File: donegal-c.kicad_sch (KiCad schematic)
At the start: 178 parts, among them J2 ISP, SW1 SW_SPST, SW10 SW_SPST, SW11 SW_SPST, SW12 SW_SPST, SW13 SW_SPST, SW14 SW_SPST, SW15 SW_SPST, SW16 SW_SPST, SW17 SW_SPST, SW18 SW_SPST, SW19 SW_SPST, SW2 SW_SPST, SW20 SW_SPST, SW21 SW_SPST, SW22 SW_SPST, SW23 SW_SPST, SW24 SW_SPST, SW25 SW_SPST, SW26 SW_SPST, SW27 SW_SPST, SW28 SW_SPST, SW29 SW_SPST, SW3 SW_SPST, SW30 SW_SPST, SW31 SW_SPST, SW32 SW_SPST, SW33 SW_SPST, SW34 SW_SPST, SW35 SW_SPST, SW36 SW_SPST, SW37 SW_SPST, SW38 SW_SPST, SW39 SW_SPST, SW4 SW_SPST, SW40 SW_SPST, SW41 SW_SPST, SW42 SW_SPST, SW43 SW_SPST, SW44 SW_SPST, SW45 SW_SPST, SW46 SW_SPST, SW47 SW_SPST, SW48 SW_SPST, SW49 SW_SPST, SW5 SW_SPST, SW50 SW_SPST, SW51 SW_SPST, SW52 SW_SPST, SW53 SW_SPST, SW54 SW_SPST, SW55 SW_SPST, SW56 SW_SPST, SW57 SW_SPST, SW58 SW_SPST, SW59 SW_SPST, SW6 SW_SPST, SW60 SW_SPST, SW61 SW_SPST, SW62 SW_SPST, SW63 SW_SPST, SW64 SW_SPST, SW65 SW_SPST, SW66 SW_SPST, SW67 SW_SPST, SW68 RESET, SW69 BOOT, SW7 SW_SPST, SW70 SW_SPST, SW71 SW_SPST, SW72 SW_SPST, SW73 SW_SPST, SW74 SW_SPST, SW75 SW_SPST, SW76 SW_SPST, SW77 SW_SPST, SW78 SW_SPST, SW79 SW_SPST, SW8 SW_SPST, SW80 SW_SPST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

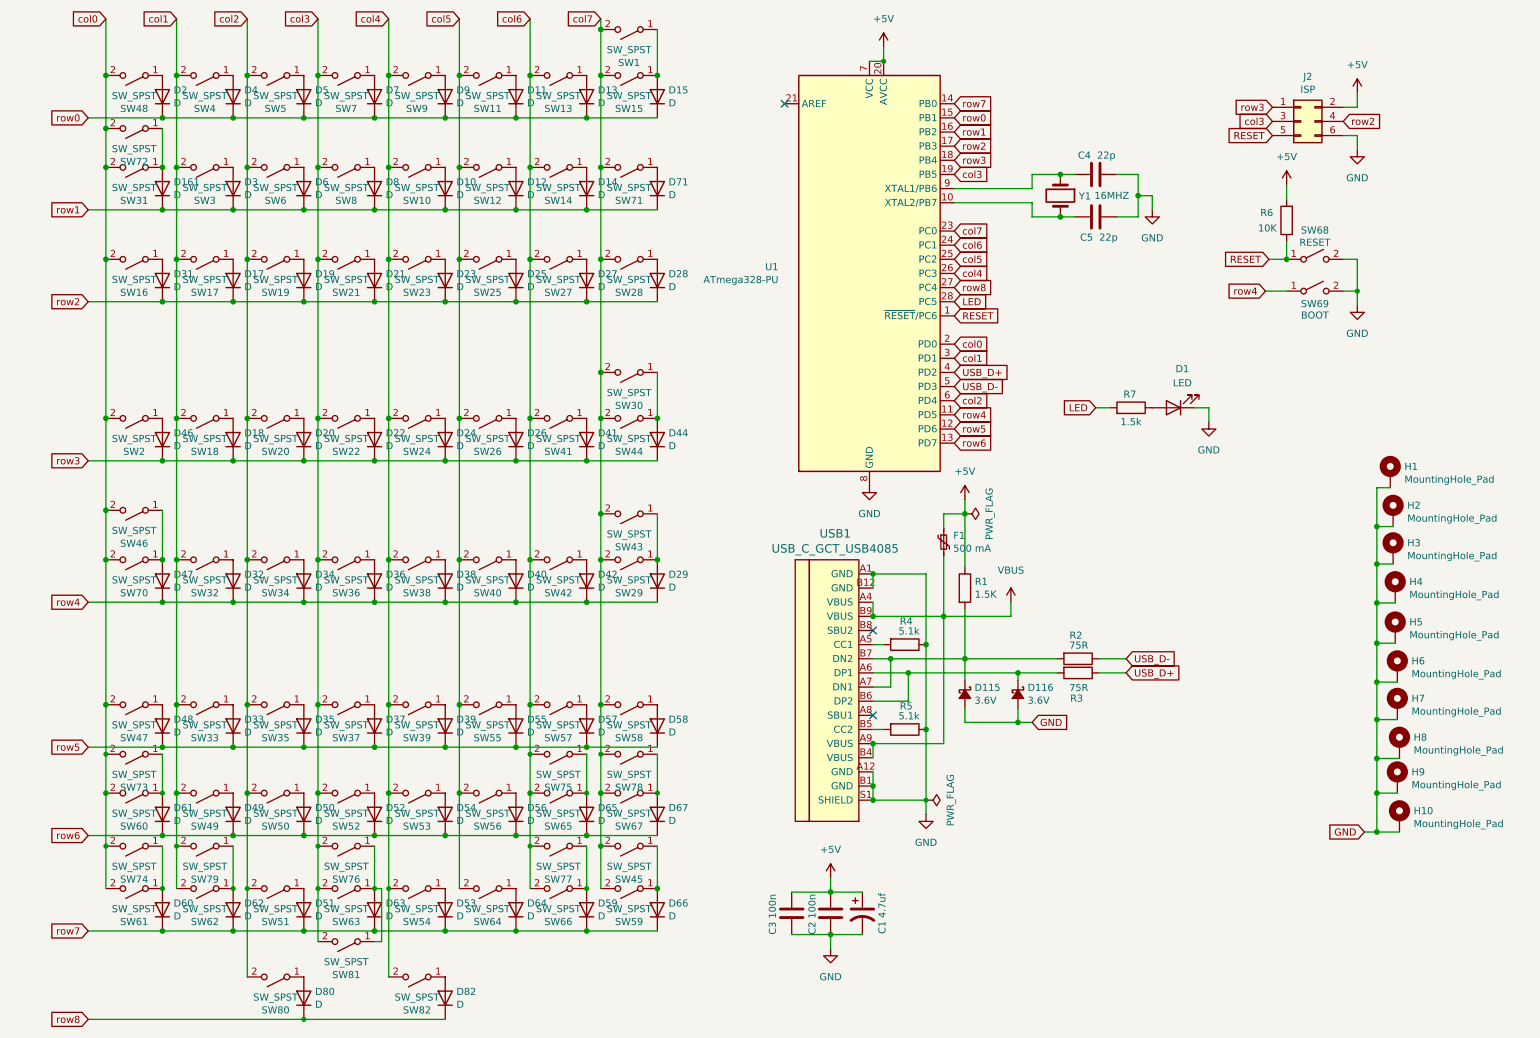
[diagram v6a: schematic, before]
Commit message: Add support for optional OLED (I/O shared with split bottom row)
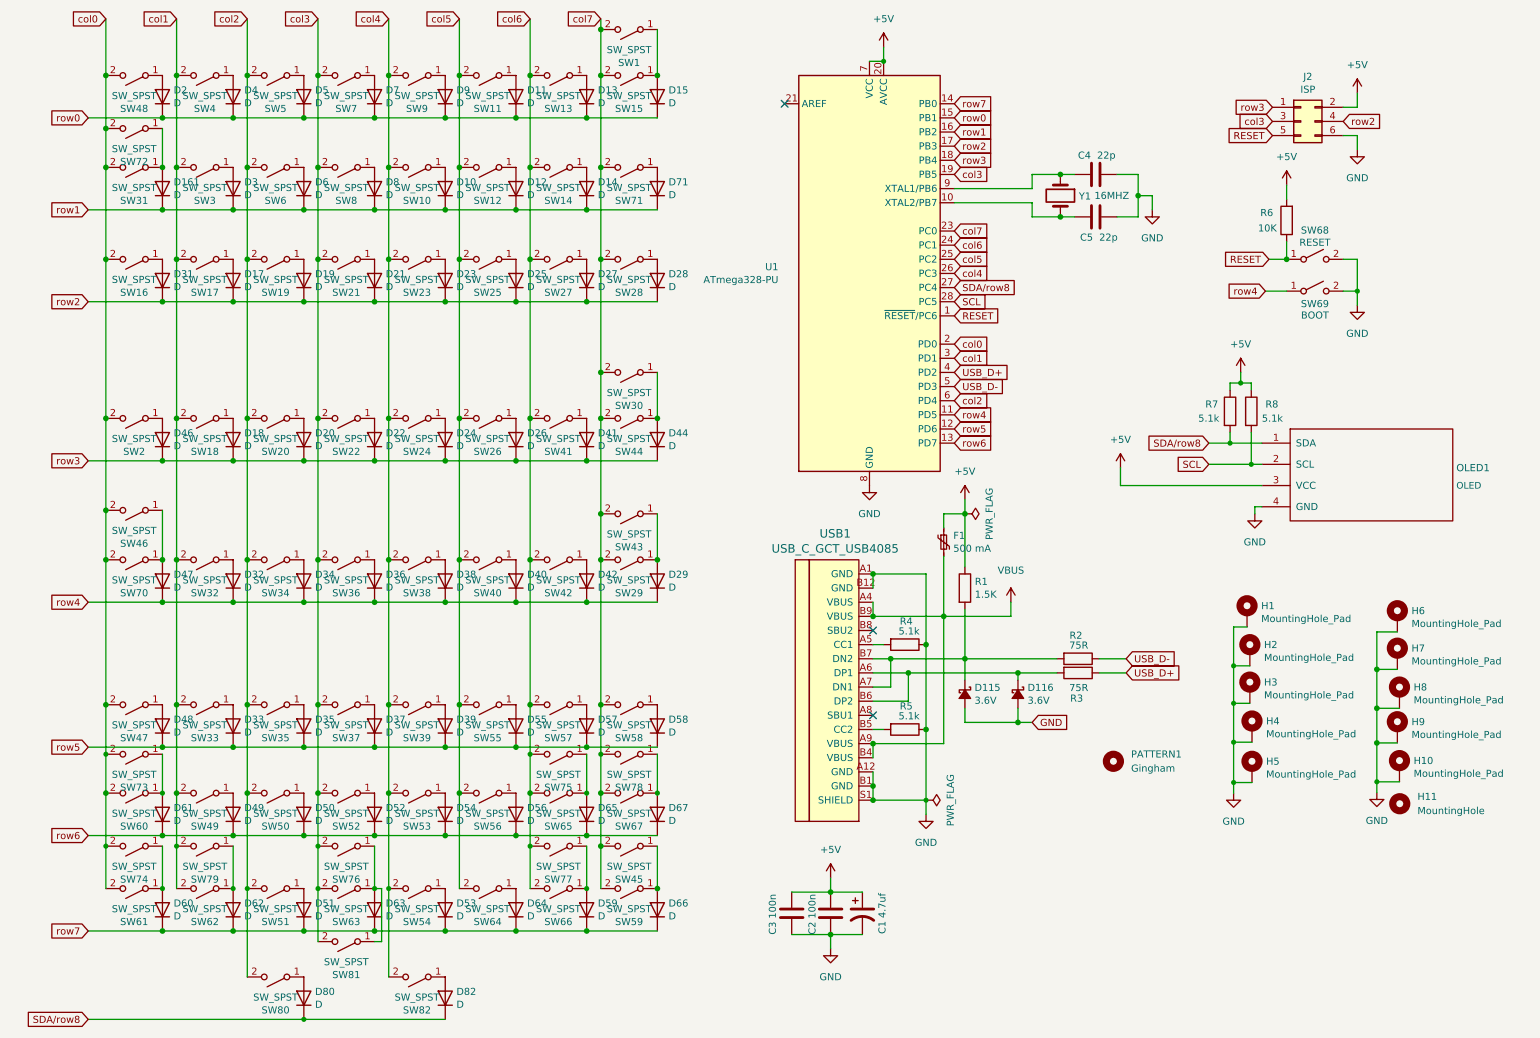
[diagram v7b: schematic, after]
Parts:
- removed D1: LED, LED_THT:LED_D3.0mm_Clear, symbol Device:LED
- added H11: MountingHole, MountingHole:MountingHole_2.2mm_M2, symbol Mechanical:MountingHole
- added OLED1: OLED, 42keebs:OLED_v2.1, symbol kbd:OLED
- added PATTERN1: Gingham, tartan:gingham, symbol Mechanical:MountingHole
- added R8: 5.1k, Resistor_THT:R_Axial_DIN0204_L3.6mm_D1.6mm_P5.08mm_Horizontal, symbol Device:R
- R7: value 1.5k -> 5.1k
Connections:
- net +5V: now also R7.1, OLED1.3 (VCC), R8.1
- net GND: now also OLED1.4 (GND)
- net LED renamed SCL
- net SCL: now also OLED1.2 (SCL), R8.2; no longer R7.2
- net row8 renamed SDA/row8
- net SDA/row8: now also R7.2, OLED1.1 (SDA)
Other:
- moved on the sheet: H1, H10, H2, H3, H4, H5, H6, H7, H8, H9

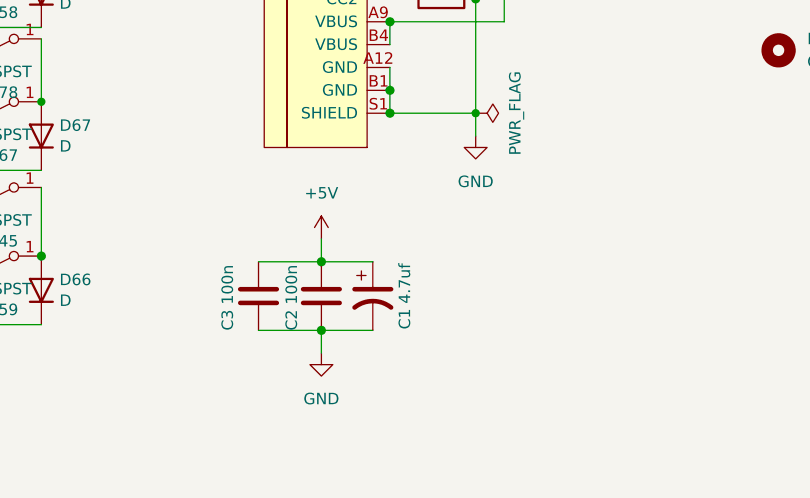
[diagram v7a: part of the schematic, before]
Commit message: Minor improvements in component positions
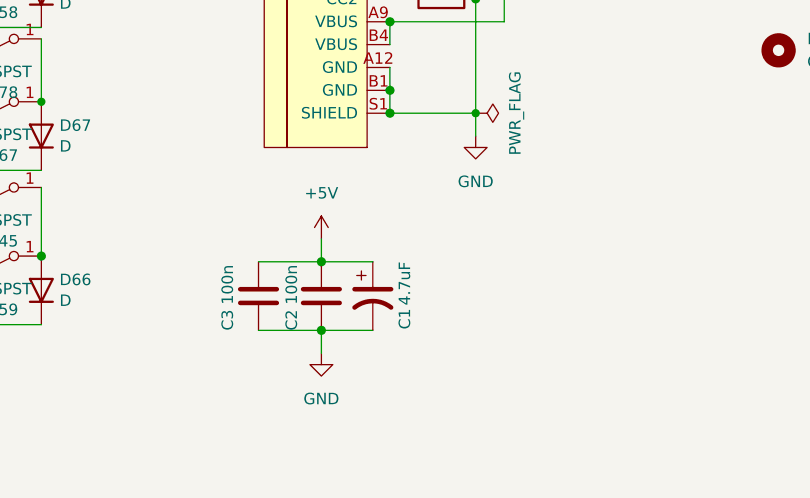
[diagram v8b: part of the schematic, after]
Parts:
- C1: value 4.7uf -> 4.7uF
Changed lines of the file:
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@@
     (in_bom yes) (on_board yes)
     (property "Reference" "C1" (id 0) (at 166.751 179.07 90))
-    (property "Value" "4.7uf" (id 1) (at 166.751 175.133 90))
+    (property "Value" "4.7uF" (id 1) (at 166.751 175.133 90))
     (property "Footprint" "Capacitor_THT:CP_Radial_D4.0mm_P1.50mm" (id 2) (at 163.195 176.53 0)
       (effects (font (size 1.27 1.27)) hide)
@@
     )
     (path "/00000000-0000-0000-0000-00005e1fb9ce"
-      (reference "C1") (unit 1) (value "4.7uf") (footprint "Capacitor_THT:CP_Radial_D4.0mm_P1.50mm")
+      (reference "C1") (unit 1) (value "4.7uF") (footprint "Capacitor_THT:CP_Radial_D4.0mm_P1.50mm")
     )
     (path "/00000000-0000-0000-0000-00005e1f9c4e"
